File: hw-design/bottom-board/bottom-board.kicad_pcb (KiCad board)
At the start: 2 copper layers, 172 x 140.5 mm, 240 parts, among them J1 RJ45_LEDS, J2 JACK_TRS_6PINS, J3 JACK_TRS_6PINS, J4 JACK_TRS_6PINS, J5 JACK_TRS_6PINS, J6 JACK_TRS_6PINS, K1 IM03, K2 IM03, P1 USB_B, P2 USB_A, P3 DIN_5, P4 DIN_5, P5 BARREL_JACK, P6 CONN_02X10, P7 CONN_01X10, P9 CONN_01X03, Q1 J112, Q10 2N7002, Q11 2N7002, Q12 2N7002, Q13 2N7002, Q14 2N7002, Q15 2N7002, Q2 J112, Q3 2N7002, Q4 2N7002, Q5 J112, Q6 J112, Q7 2N7002, Q8 2N7002, Q9 2N7002, SW1 SW_PUSH, U1 MCP1754ST-5002E/MB, U10 LM4811, U11 RT9701, U12 6N137S, U13 ISL83491, U2 KA7809, U3 NCP1117ST50T3G, U4 NCP1117ST33T3G, U5 CS4245, U6 ICnova_A20_SODIMM, U7 LM4562, U8 LM4562, U9 LM4562

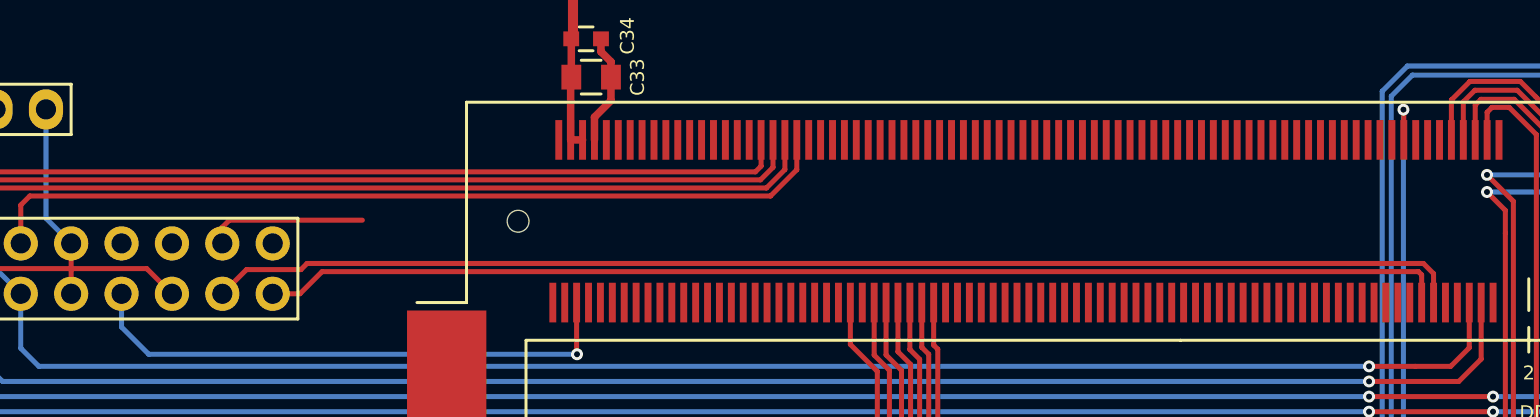
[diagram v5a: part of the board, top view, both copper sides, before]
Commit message: pcb: updating HMI tracks
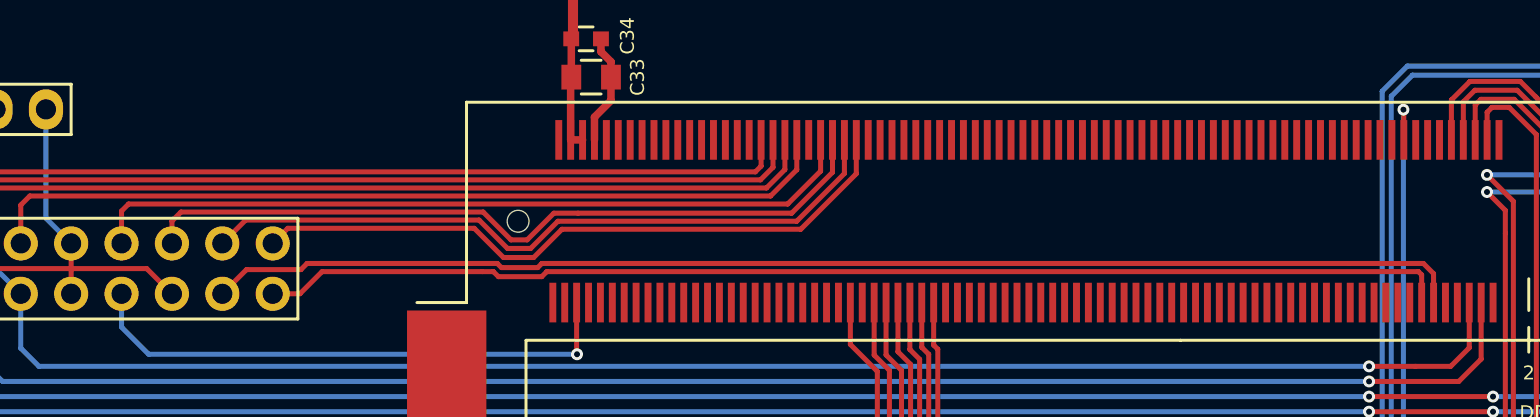
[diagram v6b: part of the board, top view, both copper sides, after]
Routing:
- net UART_RX3_HMI: track 0.00 -> 39.3 mm
- net UART_TX3_HMI: track 0.00 -> 38.2 mm
- net UART_RTS3_HMI: track 0.00 -> 33.8 mm
- net UART_CTS3_HMI: track 8.02 -> 35.7 mm
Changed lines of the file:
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@@
   (general
     (links 571)
-    (no_connects 178)
+    (no_connects 174)
     (area 60.028961 19.52224 232.128968 160.122244)
     (thickness 1.6)
     (drawings 17)
-    (tracks 1451)
+    (tracks 1489)
     (zones 0)
     (modules 240)
@@
   )
   (setup
-    (last_trace_width 0.508)
+    (last_trace_width 0.254)
     (user_trace_width 0.2032)
     (user_trace_width 0.254)
@@
   (segment (start 100.772 34.2634) (end 100.772 36.83) (width 0.508) (layer F.Cu) (net 98) (status 30))
   (segment (start 100.57826 34.06966) (end 100.772 34.2634) (width 0.508) (layer F.Cu) (net 98) (status 30))
+  (segment (start 118.1862 64.4398) (end 118.999 64.4398) (width 0.254) (layer F.Cu) (net 99))
+  (segment (start 120.3452 63.0936) (end 121.5644 63.0936) (width 0.254) (layer F.Cu) (net 99))
+  (segment (start 118.999 64.4398) (end 120.3452 63.0936) (width 0.254) (layer F.Cu) (net 99))
+  (segment (start 101.092 64.6176) (end 101.092 63.492806) (width 0.254) (layer F.Cu) (net 99) (status 400000))
+  (segment (start 116.782006 63.035606) (end 118.1862 64.4398) (width 0.254) (layer F.Cu) (net 99))
+  (segment (start 101.5492 63.035606) (end 116.782006 63.035606) (width 0.254) (layer F.Cu) (net 99))
+  (segment (start 101.092 63.492806) (end 101.5492 63.035606) (width 0.254) (layer F.Cu) (net 99))
+  (segment (start 134.3928 59.4) (end 134.3928 61.0348) (width 0.254) (layer F.Cu) (net 99) (status 400000))
+  (segment (start 132.334 63.0936) (end 121.5644 63.0936) (width 0.254) (layer F.Cu) (net 99))
+  (segment (start 134.3928 61.0348) (end 132.334 63.0936) (width 0.254) (layer F.Cu) (net 99))
+  (segment (start 98.552 64.6176) (end 98.552 62.987204) (width 0.254) (layer F.Cu) (net 100) (status 400000))
+  (segment (start 133.7928 60.9744) (end 133.7928 59.4) (width 0.254) (layer F.Cu) (net 100) (status 800000))
+  (segment (start 132.135596 62.631604) (end 133.7928 60.9744) (width 0.254) (layer F.Cu) (net 100))
+  (segment (start 98.9076 62.631604) (end 132.135596 62.631604) (width 0.254) (layer F.Cu) (net 100))
+  (segment (start 98.552 62.987204) (end 98.9076 62.631604) (width 0.254) (layer F.Cu) (net 100))
+  (segment (start 106.172 64.6176) (end 106.934 63.8556) (width 0.254) (layer F.Cu) (net 101) (status 400000))
+  (segment (start 135.5928 61.1048) (end 135.5928 59.4) (width 0.254) (layer F.Cu) (net 101) (status 800000))
+  (segment (start 132.793598 63.904002) (end 135.5928 61.1048) (width 0.254) (layer F.Cu) (net 101))
+  (segment (start 120.753998 63.904002) (end 132.793598 63.904002) (width 0.254) (layer F.Cu) (net 101))
+  (segment (start 119.3292 65.3288) (end 120.753998 63.904002) (width 0.254) (layer F.Cu) (net 101))
+  (segment (start 117.8052 65.3288) (end 119.3292 65.3288) (width 0.254) (layer F.Cu) (net 101))
+  (segment (start 116.332 63.8556) (end 117.8052 65.3288) (width 0.254) (layer F.Cu) (net 101))
+  (segment (start 106.934 63.8556) (end 116.332 63.8556) (width 0.254) (layer F.Cu) (net 101))
   (segment (start 89.662 57.8612) (end 89.662 65.8876) (width 0.254) (layer B.Cu) (net 102))
   (segment (start 89.662 65.8876) (end 90.932 67.1576) (width 0.254) (layer B.Cu) (net 102))
@@
   (segment (start 92.5576 71.5772) (end 161.4424 71.5772) (width 0.254) (layer B.Cu) (net 102))
   (segment (start 90.932 69.9516) (end 92.5576 71.5772) (width 0.254) (layer B.Cu) (net 102))
-  (segment (start 103.632 64.6176) (end 103.632 63.802402) (width 0.254) (layer F.Cu) (net 103))
-  (segment (start 103.632 63.802402) (end 103.9876 63.446802) (width 0.254) (layer F.Cu) (net 103))
-  (segment (start 103.9876 63.446802) (end 110.6932 63.446802) (width 0.254) (layer F.Cu) (net 103))
-  (segment (start 110.6932 63.446802) (end 110.6932 63.446802) (width 0.254) (layer F.Cu) (net 103))
+  (segment (start 103.632 64.6176) (end 104.809992 63.439608) (width 0.254) (layer F.Cu) (net 103) (status 400000))
+  (segment (start 134.9928 61.0952) (end 134.9928 59.4) (width 0.254) (layer F.Cu) (net 103) (status 800000))
+  (segment (start 132.588 63.5) (end 134.9928 61.0952) (width 0.254) (layer F.Cu) (net 103))
+  (segment (start 120.5484 63.5) (end 132.588 63.5) (width 0.254) (layer F.Cu) (net 103))
+  (segment (start 119.1768 64.8716) (end 120.5484 63.5) (width 0.254) (layer F.Cu) (net 103))
+  (segment (start 118.0084 64.8716) (end 119.1768 64.8716) (width 0.254) (layer F.Cu) (net 103))
+  (segment (start 116.576408 63.439608) (end 118.0084 64.8716) (width 0.254) (layer F.Cu) (net 103))
+  (segment (start 104.809992 63.439608) (end 116.576408 63.439608) (width 0.254) (layer F.Cu) (net 103))
   (segment (start 92.202 57.8612) (end 92.202 65.8876) (width 0.254) (layer B.Cu) (net 104))
   (segment (start 92.202 65.8876) (end 93.472 67.1576) (width 0.254) (layer B.Cu) (net 104))
@@
   (via (at 161.4424 70.8152) (size 0.6) (layers F.Cu B.Cu) (net 104))
   (segment (start 161.4424 70.8152) (end 163.7792 70.8152) (width 0.254) (layer F.Cu) (net 104))
+  (segment (start 116.7384 66.04) (end 117.2972 66.04) (width 0.254) (layer F.Cu) (net 105))
+  (segment (start 119.7356 66.294) (end 119.9896 66.04) (width 0.254) (layer F.Cu) (net 105))
+  (segment (start 117.5512 66.294) (end 119.7356 66.294) (width 0.254) (layer F.Cu) (net 105))
+  (segment (start 117.2972 66.04) (end 117.5512 66.294) (width 0.254) (layer F.Cu) (net 105))
+  (segment (start 115.7224 66.04) (end 116.7384 66.04) (width 0.254) (layer F.Cu) (net 105))
   (segment (start 164.0928 67.6) (end 164.0928 66.2012) (width 0.254) (layer F.Cu) (net 105))
+  (segment (start 163.9316 66.04) (end 119.9896 66.04) (width 0.254) (layer F.Cu) (net 105))
+  (segment (start 164.0928 66.2012) (end 163.9316 66.04) (width 0.254) (layer F.Cu) (net 105))
   (segment (start 107.5436 67.1576) (end 106.172 67.1576) (width 0.254) (layer F.Cu) (net 105))
   (segment (start 108.6612 66.04) (end 107.5436 67.1576) (width 0.254) (layer F.Cu) (net 105))
-  (segment (start 163.9316 66.04) (end 108.6612 66.04) (width 0.254) (layer F.Cu) (net 105))
-  (segment (start 164.0928 66.2012) (end 163.9316 66.04) (width 0.254) (layer F.Cu) (net 105))
+  (segment (start 115.7224 66.04) (end 108.6612 66.04) (width 0.254) (layer F.Cu) (net 105))
   (segment (start 98.552 67.1576) (end 98.552 68.834) (width 0.254) (layer B.Cu) (net 106))
   (segment (start 121.4928 70.1848) (end 121.4928 67.6) (width 0.254) (layer F.Cu) (net 106))
@@
   (segment (start 99.9236 70.2056) (end 121.5136 70.2056) (width 0.254) (layer B.Cu) (net 106))
   (segment (start 98.552 68.834) (end 99.9236 70.2056) (width 0.254) (layer B.Cu) (net 106))
-  (segment (start 160.4264 65.628804) (end 107.903996 65.628804) (width 0.254) (layer F.Cu) (net 107))
+  (segment (start 116.1288 65.628804) (end 117.495604 65.628804) (width 0.254) (layer F.Cu) (net 107))
+  (segment (start 119.5324 65.8368) (end 119.740396 65.628804) (width 0.254) (layer F.Cu) (net 107))
+  (segment (start 117.7036 65.8368) (end 119.5324 65.8368) (width 0.254) (layer F.Cu) (net 107))
+  (segment (start 117.495604 65.628804) (end 117.7036 65.8368) (width 0.254) (layer F.Cu) (net 107))
+  (segment (start 160.4264 65.628804) (end 119.740396 65.628804) (width 0.254) (layer F.Cu) (net 107))
+  (segment (start 116.1288 65.628804) (end 107.903996 65.628804) (width 0.254) (layer F.Cu) (net 107))
   (segment (start 104.8512 65.9384) (end 103.632 67.1576) (width 0.254) (layer F.Cu) (net 107))
   (segment (start 107.5944 65.9384) (end 104.8512 65.9384) (width 0.254) (layer F.Cu) (net 107))

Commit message: exchanging more I/Os to make easy the layout
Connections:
- U6 pad 172: Net-(U6-Pad172) -> RIGHT_BYPASS_CTRL
- U6 pad 174: Net-(U6-Pad174) -> LEFT_BYPASS_CTRL
- U6 pad 176: Net-(U6-Pad176) -> HP_UP/DN
- U6 pad 178: Net-(U6-Pad178) -> HP_CLOCK
- U6 pad 184: Net-(U6-Pad184) -> UART_TX4_MIDI
- U6 pad 186: Net-(U6-Pad186) -> UART_RX4_MIDI
- U6 pad 20: UART_TX4_MIDI -> Net-(U6-Pad20)
- U6 pad 22: UART_RX4_MIDI -> Net-(U6-Pad22)
- U6 pad 76: RIGHT_BYPASS_CTRL -> Net-(U6-Pad76)
- U6 pad 78: LEFT_BYPASS_CTRL -> Net-(U6-Pad78)
- U6 pad 82: HP_CLOCK -> Net-(U6-Pad82)
- U6 pad 84: HP_UP/DN -> Net-(U6-Pad84)
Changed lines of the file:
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@@
     (pad_to_mask_clearance 0)
     (aux_axis_origin 75.5777 23.0759)
-    (visible_elements FFFFF77F)
+    (visible_elements FFFFFF7F)
     (pcbplotparams
       (layerselection 0x3ffff_80000001)
@@
   (net 297 "Net-(U6-Pad168)")
   (net 298 "Net-(U6-Pad170)")
-  (net 299 "Net-(U6-Pad172)")
-  (net 300 "Net-(U6-Pad174)")
-  (net 301 "Net-(U6-Pad176)")
-  (net 302 "Net-(U6-Pad178)")
-  (net 303 "Net-(U6-Pad180)")
-  (net 304 "Net-(U6-Pad182)")
-  (net 305 "Net-(U6-Pad184)")
-  (net 306 "Net-(U6-Pad186)")
-  (net 307 "Net-(U6-Pad188)")
-  (net 308 "Net-(U6-Pad192)")
-  (net 309 "Net-(U6-Pad194)")
-  (net 310 "Net-(U6-Pad198)")
-  (net 311 "Net-(U12-Pad7)")
+  (net 299 "Net-(U6-Pad180)")
+  (net 300 "Net-(U6-Pad182)")
+  (net 301 "Net-(U6-Pad188)")
+  (net 302 "Net-(U6-Pad192)")
+  (net 303 "Net-(U6-Pad194)")
+  (net 304 "Net-(U6-Pad198)")
+  (net 305 "Net-(U12-Pad7)")
+  (net 306 "Net-(U6-Pad20)")
+  (net 307 "Net-(U6-Pad22)")
+  (net 308 "Net-(U6-Pad76)")
+  (net 309 "Net-(U6-Pad78)")
+  (net 310 "Net-(U6-Pad82)")
+  (net 311 "Net-(U6-Pad84)")
   (net_class Default "This is the default net class."
     (clearance 0.15)
@@
     (add_net "Net-(U6-Pad170)")
     (add_net "Net-(U6-Pad171)")
-    (add_net "Net-(U6-Pad172)")
     (add_net "Net-(U6-Pad173)")
-    (add_net "Net-(U6-Pad174)")
     (add_net "Net-(U6-Pad175)")
-    (add_net "Net-(U6-Pad176)")
-    (add_net "Net-(U6-Pad178)")
     (add_net "Net-(U6-Pad179)")
     (add_net "Net-(U6-Pad180)")
     (add_net "Net-(U6-Pad181)")
     (add_net "Net-(U6-Pad182)")
-    (add_net "Net-(U6-Pad184)")
     (add_net "Net-(U6-Pad185)")
-    (add_net "Net-(U6-Pad186)")
     (add_net "Net-(U6-Pad187)")
     (add_net "Net-(U6-Pad188)")
@@
     (add_net "Net-(U6-Pad198)")
     (add_net "Net-(U6-Pad2)")
+    (add_net "Net-(U6-Pad20)")
     (add_net "Net-(U6-Pad21)")
+    (add_net "Net-(U6-Pad22)")
     (add_net "Net-(U6-Pad25)")
     (add_net "Net-(U6-Pad27)")
@@
     (add_net "Net-(U6-Pad72)")
     (add_net "Net-(U6-Pad75)")
+    (add_net "Net-(U6-Pad76)")
     (add_net "Net-(U6-Pad77)")
+    (add_net "Net-(U6-Pad78)")
     (add_net "Net-(U6-Pad8)")
     (add_net "Net-(U6-Pad81)")
+    (add_net "Net-(U6-Pad82)")
     (add_net "Net-(U6-Pad83)")
+    (add_net "Net-(U6-Pad84)")
     (add_net "Net-(U6-Pad87)")
     (add_net "Net-(U6-Pad88)")
@@
       (net 162 UART_RE_CHAIN))
     (pad 20 smd rect (at -25.95 -4.1 180) (size 0.35 2) (layers F.Cu F.Paste F.Mask)
-      (net 146 UART_TX4_MIDI))
+      (net 306 "Net-(U6-Pad20)"))
     (pad 22 smd rect (at -25.35 -4.1 180) (size 0.35 2) (layers F.Cu F.Paste F.Mask)
-      (net 74 UART_RX4_MIDI))
+      (net 307 "Net-(U6-Pad22)"))
     (pad 24 smd rect (at -24.75 -4.1 180) (size 0.35 2) (layers F.Cu F.Paste F.Mask)
       (net 171 RFU_02_HMI))
@@
       (net 6 GNDD))
     (pad 76 smd rect (at -5.55 -4.1 180) (size 0.35 2) (layers F.Cu F.Paste F.Mask)
-      (net 143 RIGHT_BYPASS_CTRL))
+      (net 308 "Net-(U6-Pad76)"))
     (pad 78 smd rect (at -4.95 -4.1 180) (size 0.35 2) (layers F.Cu F.Paste F.Mask)
-      (net 142 LEFT_BYPASS_CTRL))
+      (net 309 "Net-(U6-Pad78)"))
     (pad 80 smd rect (at -4.35 -4.1 180) (size 0.35 2) (layers F.Cu F.Paste F.Mask)
       (net 6 GNDD))
     (pad 82 smd rect (at -3.75 -4.1 180) (size 0.35 2) (layers F.Cu F.Paste F.Mask)
-      (net 163 HP_CLOCK))
+      (net 310 "Net-(U6-Pad82)"))
     (pad 84 smd rect (at -3.15 -4.1 180) (size 0.35 2) (layers F.Cu F.Paste F.Mask)
-      (net 164 HP_UP/DN))
+      (net 311 "Net-(U6-Pad84)"))
     (pad 86 smd rect (at -2.55 -4.1 180) (size 0.35 2) (layers F.Cu F.Paste F.Mask)
       (net 6 GNDD))
@@
       (net 298 "Net-(U6-Pad170)"))
     (pad 172 smd rect (at 23.25 -4.1 180) (size 0.35 2) (layers F.Cu F.Paste F.Mask)
-      (net 299 "Net-(U6-Pad172)"))
+      (net 143 RIGHT_BYPASS_CTRL))
     (pad 174 smd rect (at 23.85 -4.1 180) (size 0.35 2) (layers F.Cu F.Paste F.Mask)
-      (net 300 "Net-(U6-Pad174)"))
+      (net 142 LEFT_BYPASS_CTRL))
     (pad 176 smd rect (at 24.45 -4.1 180) (size 0.35 2) (layers F.Cu F.Paste F.Mask)
-      (net 301 "Net-(U6-Pad176)"))
+      (net 164 HP_UP/DN))
     (pad 178 smd rect (at 25.05 -4.1 180) (size 0.35 2) (layers F.Cu F.Paste F.Mask)
-      (net 302 "Net-(U6-Pad178)"))
+      (net 163 HP_CLOCK))
     (pad 180 smd rect (at 25.65 -4.1 180) (size 0.35 2) (layers F.Cu F.Paste F.Mask)
-      (net 303 "Net-(U6-Pad180)"))
+      (net 299 "Net-(U6-Pad180)"))
     (pad 182 smd rect (at 26.25 -4.1 180) (size 0.35 2) (layers F.Cu F.Paste F.Mask)
-      (net 304 "Net-(U6-Pad182)"))
+      (net 300 "Net-(U6-Pad182)"))
     (pad 184 smd rect (at 26.85 -4.1 180) (size 0.35 2) (layers F.Cu F.Paste F.Mask)
-      (net 305 "Net-(U6-Pad184)"))
+      (net 146 UART_TX4_MIDI))
     (pad 186 smd rect (at 27.45 -4.1 180) (size 0.35 2) (layers F.Cu F.Paste F.Mask)
-      (net 306 "Net-(U6-Pad186)"))
+      (net 74 UART_RX4_MIDI))
     (pad 188 smd rect (at 28.05 -4.1 180) (size 0.35 2) (layers F.Cu F.Paste F.Mask)
-      (net 307 "Net-(U6-Pad188)"))
+      (net 301 "Net-(U6-Pad188)"))
     (pad 190 smd rect (at 28.65 -4.1 180) (size 0.35 2) (layers F.Cu F.Paste F.Mask)
       (net 6 GNDD))
     (pad 192 smd rect (at 29.25 -4.1 180) (size 0.35 2) (layers F.Cu F.Paste F.Mask)
-      (net 308 "Net-(U6-Pad192)"))
+      (net 302 "Net-(U6-Pad192)"))
     (pad 194 smd rect (at 29.85 -4.1 180) (size 0.35 2) (layers F.Cu F.Paste F.Mask)
-      (net 309 "Net-(U6-Pad194)"))
+      (net 303 "Net-(U6-Pad194)"))
     (pad 196 smd rect (at 30.45 -4.1 180) (size 0.35 2) (layers F.Cu F.Paste F.Mask)
       (net 106 POWER_BUTTON))
     (pad 198 smd rect (at 31.05 -4.1 180) (size 0.35 2) (layers F.Cu F.Paste F.Mask)
-      (net 310 "Net-(U6-Pad198)"))
+      (net 304 "Net-(U6-Pad198)"))
     (pad 200 smd rect (at 31.65 -4.1 180) (size 0.35 2) (layers F.Cu F.Paste F.Mask)
       (net 137 UBOOT_BUTTON))
@@
       (net 73 "Net-(D16-Pad1)"))
     (pad 7 smd rect (at -1.27 -3.81 180) (size 1.524 2.032) (layers F.Cu F.Paste F.Mask)
-      (net 311 "Net-(U12-Pad7)"))
+      (net 305 "Net-(U12-Pad7)"))
     (pad 8 smd rect (at -3.81 -3.81 180) (size 1.524 2.032) (layers F.Cu F.Paste F.Mask)
       (net 7 +5V))
@@
   (segment (start 120.3452 63.0936) (end 121.5644 63.0936) (width 0.254) (layer F.Cu) (net 99))
   (segment (start 118.999 64.4398) (end 120.3452 63.0936) (width 0.254) (layer F.Cu) (net 99))
-  (segment (start 101.092 64.6176) (end 101.092 63.492806) (width 0.254) (layer F.Cu) (net 99) (status 400000))
+  (segment (start 101.092 64.6176) (end 101.092 63.492806) (width 0.254) (layer F.Cu) (net 99))
   (segment (start 116.782006 63.035606) (end 118.1862 64.4398) (width 0.254) (layer F.Cu) (net 99))
   (segment (start 101.5492 63.035606) (end 116.782006 63.035606) (width 0.254) (layer F.Cu) (net 99))
   (segment (start 101.092 63.492806) (end 101.5492 63.035606) (width 0.254) (layer F.Cu) (net 99))
-  (segment (start 134.3928 59.4) (end 134.3928 61.0348) (width 0.254) (layer F.Cu) (net 99) (status 400000))
+  (segment (start 134.3928 59.4) (end 134.3928 61.0348) (width 0.254) (layer F.Cu) (net 99))
   (segment (start 132.334 63.0936) (end 121.5644 63.0936) (width 0.254) (layer F.Cu) (net 99))
   (segment (start 134.3928 61.0348) (end 132.334 63.0936) (width 0.254) (layer F.Cu) (net 99))
-  (segment (start 98.552 64.6176) (end 98.552 62.987204) (width 0.254) (layer F.Cu) (net 100) (status 400000))
-  (segment (start 133.7928 60.9744) (end 133.7928 59.4) (width 0.254) (layer F.Cu) (net 100) (status 800000))
+  (segment (start 98.552 64.6176) (end 98.552 62.987204) (width 0.254) (layer F.Cu) (net 100))
+  (segment (start 133.7928 60.9744) (end 133.7928 59.4) (width 0.254) (layer F.Cu) (net 100))
   (segment (start 132.135596 62.631604) (end 133.7928 60.9744) (width 0.254) (layer F.Cu) (net 100))
   (segment (start 98.9076 62.631604) (end 132.135596 62.631604) (width 0.254) (layer F.Cu) (net 100))
   (segment (start 98.552 62.987204) (end 98.9076 62.631604) (width 0.254) (layer F.Cu) (net 100))
-  (segment (start 106.172 64.6176) (end 106.934 63.8556) (width 0.254) (layer F.Cu) (net 101) (status 400000))
-  (segment (start 135.5928 61.1048) (end 135.5928 59.4) (width 0.254) (layer F.Cu) (net 101) (status 800000))
+  (segment (start 106.172 64.6176) (end 106.934 63.8556) (width 0.254) (layer F.Cu) (net 101))
+  (segment (start 135.5928 61.1048) (end 135.5928 59.4) (width 0.254) (layer F.Cu) (net 101))
   (segment (start 132.793598 63.904002) (end 135.5928 61.1048) (width 0.254) (layer F.Cu) (net 101))
   (segment (start 120.753998 63.904002) (end 132.793598 63.904002) (width 0.254) (layer F.Cu) (net 101))
@@
   (segment (start 92.5576 71.5772) (end 161.4424 71.5772) (width 0.254) (layer B.Cu) (net 102))
   (segment (start 90.932 69.9516) (end 92.5576 71.5772) (width 0.254) (layer B.Cu) (net 102))
-  (segment (start 103.632 64.6176) (end 104.809992 63.439608) (width 0.254) (layer F.Cu) (net 103) (status 400000))
-  (segment (start 134.9928 61.0952) (end 134.9928 59.4) (width 0.254) (layer F.Cu) (net 103) (status 800000))
+  (segment (start 103.632 64.6176) (end 104.809992 63.439608) (width 0.254) (layer F.Cu) (net 103))
+  (segment (start 134.9928 61.0952) (end 134.9928 59.4) (width 0.254) (layer F.Cu) (net 103))
   (segment (start 132.588 63.5) (end 134.9928 61.0952) (width 0.254) (layer F.Cu) (net 103))
   (segment (start 120.5484 63.5) (end 132.588 63.5) (width 0.254) (layer F.Cu) (net 103))
